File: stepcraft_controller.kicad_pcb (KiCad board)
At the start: 2 copper layers, 68 x 55 mm, 67 parts, among them J1 USB, J2 Probe, J3 Spindle, J4 CONN_01X03, J5 CONN_01X03, J6 Relay select, J7 Serial, J8 ISP, J9 X1, SW1 RST, U1 CP2102, U2 ADuM1201BR, U3 ADuM1201BR, U4 ATMEGA328P-AU, Y1 Crystal

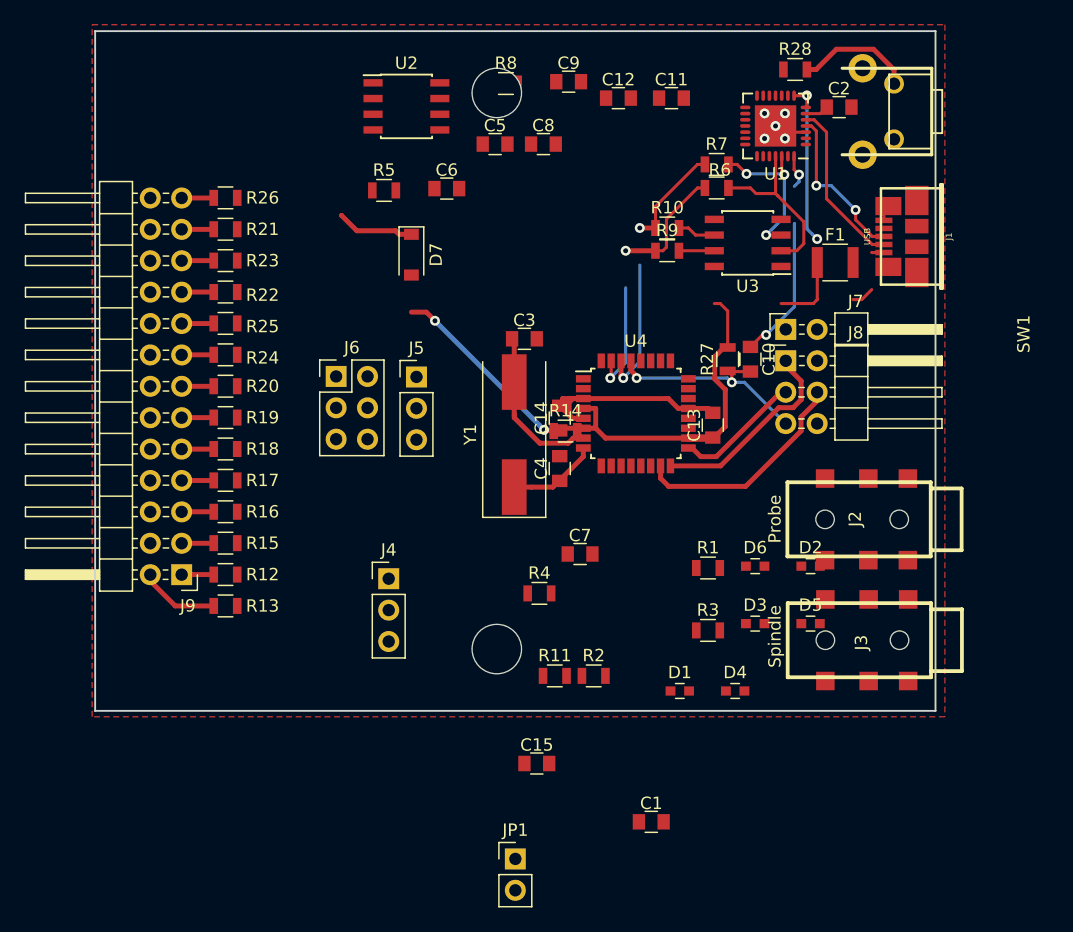
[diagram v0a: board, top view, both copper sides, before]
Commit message: Update schematics and board, fully routed board
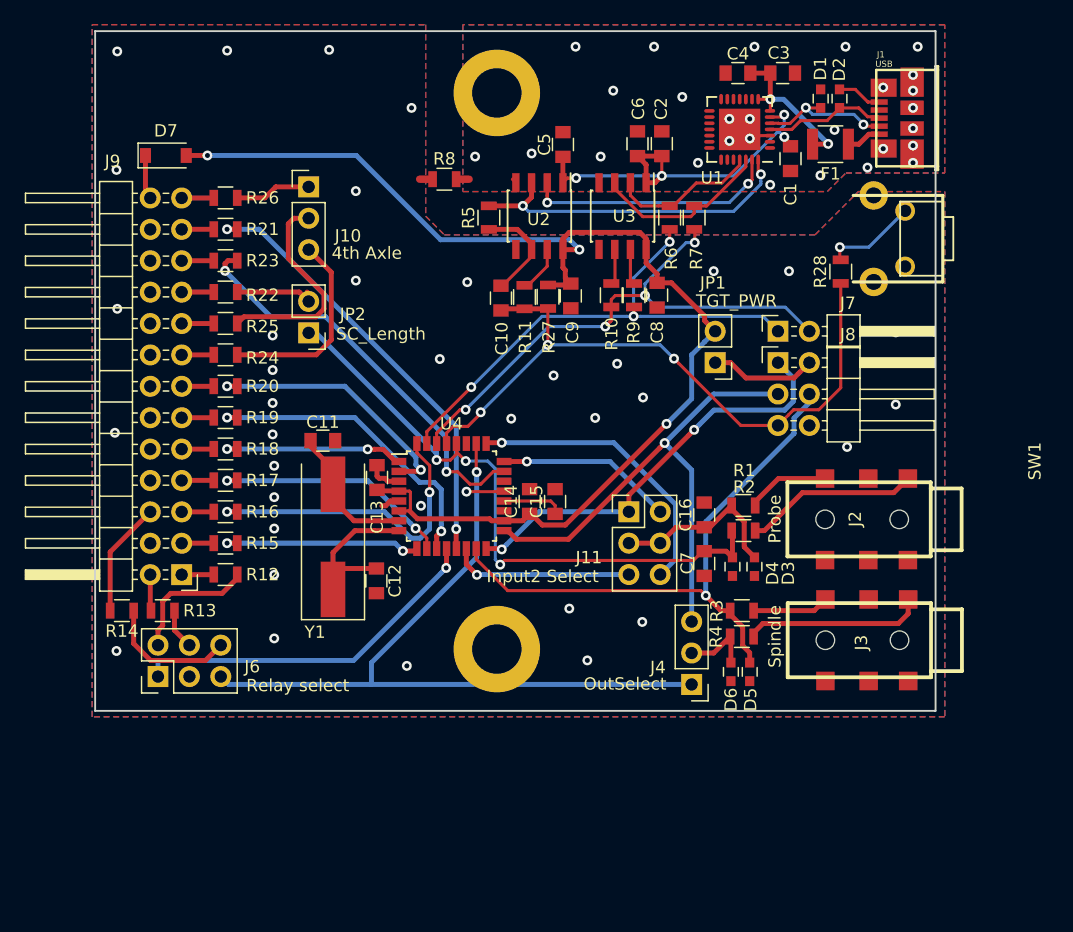
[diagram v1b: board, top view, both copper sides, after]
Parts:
- removed J5: CONN_01X03, Pin_Headers:Pin_Header_Straight_1x03_Pitch2.54mm
- added C16: 100n, Capacitors_SMD:C_0805, F.Cu at (189.3, 124.2)
- added J10: 4th Axle, Pin_Headers:Pin_Header_Straight_1x03_Pitch2.54mm, F.Cu at (157.3, 97.6)
- added J11: Input2 Select, Pin_Headers:Pin_Header_Straight_2x03_Pitch2.54mm, F.Cu at (183.2, 123.9)
- added JP2: SC_Length, Pin_Headers:Pin_Header_Straight_1x02_Pitch2.54mm, F.Cu at (157.3, 109.4)
- J1: footprint w_conn_pc:conn_usb_B_micro_smd -> iotta_footprints:conn_usb_B_micro_smd
- J4: value CONN_01X03 -> OutSelect
- moved C1 54.8 mm to (196.3, 95.3), turned to 270 degrees
- moved D1 49.3 mm to (198.7, 90.5), turned to 270 degrees
- moved C12 43.7 mm to (162.8, 129.5), turned to 270 degrees
- moved JP1 43.3 mm to (190.2, 111.8), turned to 180 degrees
- moved C11 39.5 mm to (158.4, 118.2)
- moved R14 38.7 mm to (142.2, 131.9), turned to 180 degrees
- moved D2 37.9 mm to (200.2, 90.5), turned to 270 degrees
- moved C4 35.1 mm to (192.0, 88.4), turned to 180 degrees
- moved R11 30.8 mm to (174.7, 106.5), turned to 270 degrees
- moved C3 30.0 mm to (195.6, 88.4)
- moved J6 28.2 mm to (145.1, 137.2), turned to 90 degrees
- moved C13 27.5 mm to (162.8, 121.1)
- moved J4 26.0 mm to (188.3, 137.9), turned to 180 degrees
- moved D7 21.4 mm to (145.7, 95.1), turned to 0 degrees
- moved C15 21.2 mm to (177.2, 123.1), turned to 90 degrees
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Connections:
- net Net-(C1-Pad1) renamed +5VP
- D3 pad 1: Net-(D3-Pad1) -> /Input2
- D4 pad 1: /Probe -> /A5
- D5 pad 1: /SpinPWM -> /D11_MOSI
- J2 pad 1: /Probe -> Net-(J2-Pad1)
- J2 pad 2: Net-(D3-Pad1) -> Net-(J2-Pad2)
- J3 pad 1: /SpinDir/Cool -> Net-(J3-Pad1)
- J3 pad 2: /SpinPWM -> Net-(J3-Pad2)
- J4 pad 2: Net-(J4-Pad2) -> /SpinDir/Cool
- J4 pad 3: /D13 -> /D13_SCK
- R1 pad 1: Net-(D3-Pad1) -> Net-(J2-Pad2)
- R1 pad 2: Net-(J5-Pad2) -> /Input2
- R2 pad 1: /Probe -> Net-(J2-Pad1)
- R21 pad 1: /D5 -> /D9
- R23 pad 1: Net-(R23-Pad1) -> /A0
- R3 pad 1: /SpinPWM -> Net-(J3-Pad2)
- R3 pad 2: /D11 -> /D11_MOSI
- R4 pad 1: /SpinDir/Cool -> Net-(J3-Pad1)
- R4 pad 2: Net-(J4-Pad2) -> /SpinDir/Cool
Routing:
- net /A3: track 0.00 -> 61.4 mm, vias 0 -> 1
- net +5V: track 44.4 -> 99.2 mm, vias 2 -> 3
- net /A5: track 0.00 -> 51.6 mm, vias 0 -> 3
- net /D9: track 0.00 -> 35.9 mm, vias 0 -> 2
- net /A0: track 0.00 -> 33.4 mm, vias 0 -> 2
- net /D13_SCK: track 10.3 -> 42.7 mm, vias 0 -> 1
- net +5VP: track 1.91 -> 34.2 mm, vias 0 -> 4
- net /D11_MOSI: track 18.2 -> 47.8 mm, vias 0 -> 1
- net /D8: track 0.00 -> 29.3 mm, vias 0 -> 1
- net /AVR_RX: track 19.6 -> 45.6 mm, vias 2 -> 4
- net /D2: track 0.00 -> 25.7 mm, vias 0 -> 2
- net /D7: track 0.00 -> 25.5 mm, vias 0 -> 2
- net /AVR_RST: track 29.7 -> 55.1 mm
- net Net-(R5-Pad2): track 2.76 -> 27.3 mm, vias 1 -> 2
- net /AVR_TX: track 19.1 -> 42.8 mm, vias 2 -> 3
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- added copper zone on F.Cu, net +5VP
- added copper zone on B.Cu, net GND
- added copper zone on F.Cu, net GND
- added copper zone on B.Cu, net GNDD

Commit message: Update PCB routing.
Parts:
- added REF**: Symbol_CreativeCommons_CopperTop_Type2_Small, Symbols:Symbol_CreativeCommons_CopperTop_Type2_Small, B.Cu at (146.4, 90.5)
- added REF**: Symbol_CC-Attribution_CopperTop_Small, Symbols:Symbol_CC-Attribution_CopperTop_Small, B.Cu at (159.1, 90.5)
- added REF**: Symbol_CC-Noncommercial_CopperTop_Small, Symbols:Symbol_CC-Noncommercial_CopperTop_Small, B.Cu at (152.7, 90.5)
- added REF***: OSHW-Symbol_6.7x6mm_SilkScreen, Symbols:OSHW-Symbol_6.7x6mm_SilkScreen, F.Cu at (180.4, 115.9)
- JP1: value TGT_PWR -> ISP_PWR
- SW1: value RST -> Reset
- moved F1 5.17 mm to (199.9, 89.0)
- moved J4 2.54 mm to (185.7, 137.9)
- moved D1 2.09 mm to (198.8, 92.6)
- moved D2 2.08 mm to (200.3, 92.6)
- moved C1 0.54 mm to (196.2, 95.9)
- moved C13 0.13 mm to (162.8, 121.3)
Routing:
- net Net-(F1-Pad2): track 2.83 -> 10.5 mm, vias 0 -> 2
- net /A3: track 61.4 -> 54.2 mm
- net GNDD: track 8.80 -> 14.7 mm, vias 37 -> 41
- net /SpinDir/Cool: track 5.80 -> 8.64 mm
- net /D4: track 21.5 -> 23.8 mm
- net /A5: track 51.6 -> 53.3 mm
- net /D7: track 25.5 -> 27.2 mm
- net Net-(U1-Pad27): track 22.1 -> 20.8 mm
- net /D13_SCK: track 42.7 -> 43.7 mm
- net /D9: track 35.9 -> 36.7 mm
- net Net-(R5-Pad2): track 27.3 -> 26.5 mm
- net /AVR_TX: track 42.8 -> 43.4 mm
- net +5VP: track 34.2 -> 34.8 mm
- net /A0: track 33.4 -> 34.1 mm
- net /AVR_RX: track 45.6 -> 45.0 mm
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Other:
- net class Default: clearance 0 -> 0.19
- rule trace_clearance: 0 -> 0.19
- board text added: "Rev 1.0 2017"
- board text added: "SC100 Drop-in replacement"
- board text added: "Stepcraft GRBLizer"

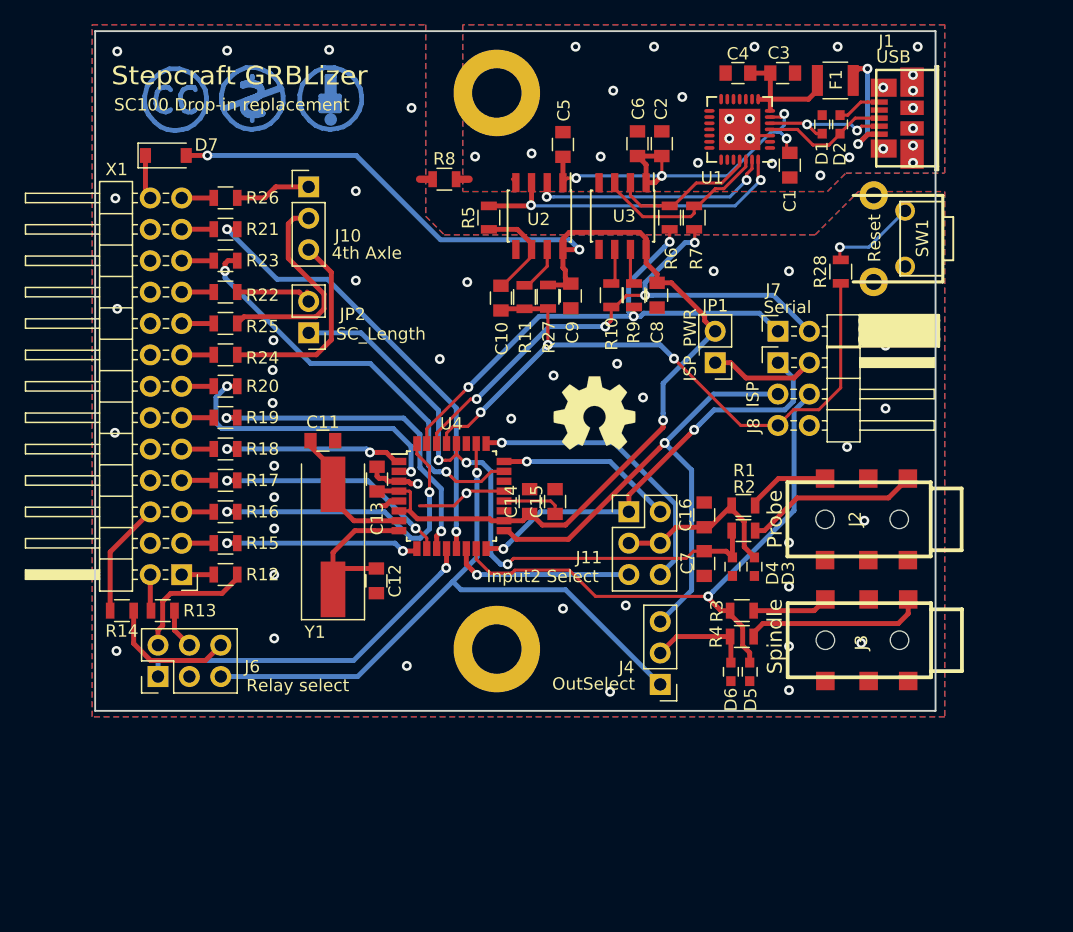
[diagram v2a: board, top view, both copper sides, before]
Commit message: Fix net name (D13), improved routing, ground plane continuity.
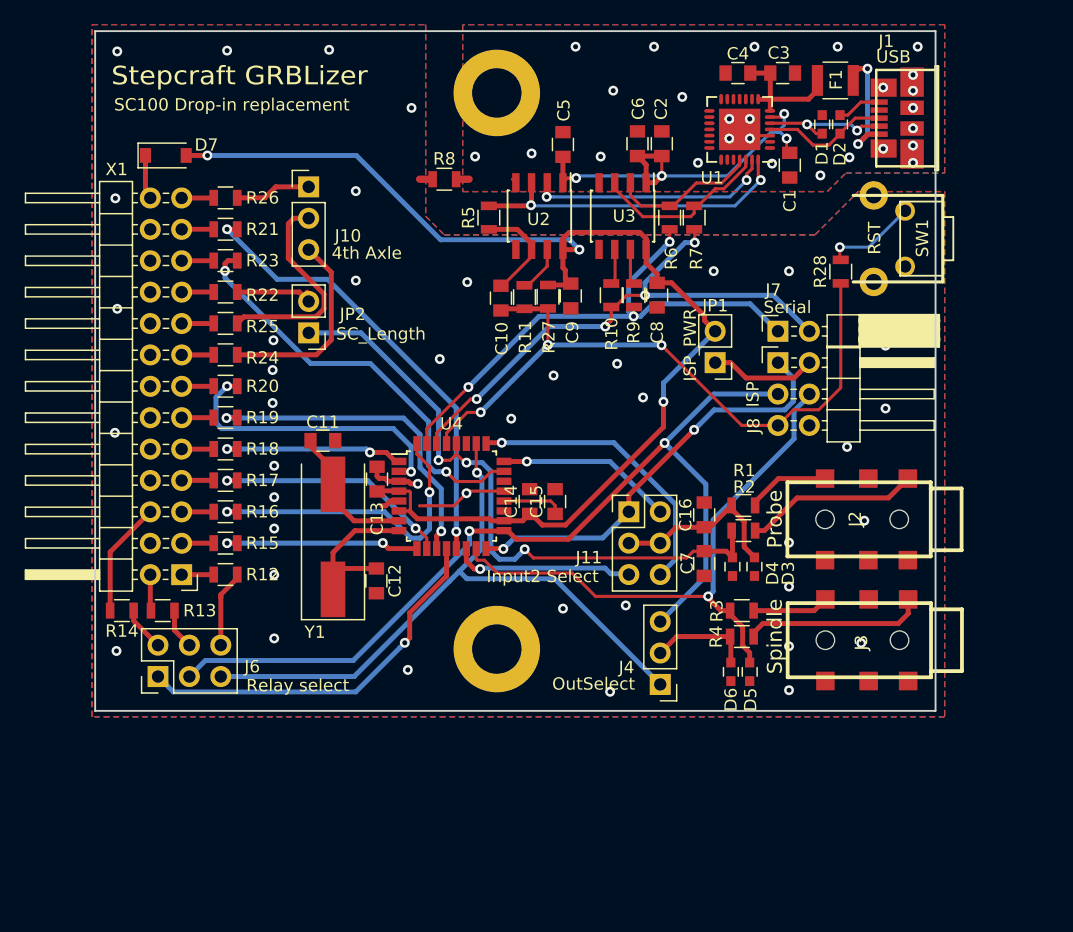
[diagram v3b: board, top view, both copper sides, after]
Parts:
- removed REF**: Symbol_CreativeCommons_CopperTop_Type2_Small, Symbols:Symbol_CreativeCommons_CopperTop_Type2_Small
- removed REF**: Symbol_CC-Attribution_CopperTop_Small, Symbols:Symbol_CC-Attribution_CopperTop_Small
- removed REF**: Symbol_CC-Noncommercial_CopperTop_Small, Symbols:Symbol_CC-Noncommercial_CopperTop_Small
- removed REF***: OSHW-Symbol_6.7x6mm_SilkScreen, Symbols:OSHW-Symbol_6.7x6mm_SilkScreen
- SW1: value Reset -> RST
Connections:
- J6 pad 3: /D13 -> /D13_SCK
- R12 pad 1: Net-(J6-Pad2) -> Net-(J6-Pad6)
- R14 pad 1: Net-(J6-Pad6) -> Net-(J6-Pad2)
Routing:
- net /D13_SCK: track 43.7 -> 75.7 mm, vias 1 -> 2
- net Net-(J6-Pad2): track 10.8 -> 3.61 mm
- net Net-(J6-Pad6): track 10.8 -> 6.27 mm
- net /D8: track 29.3 -> 31.2 mm
- net /AVR_TX: track 43.4 -> 44.1 mm

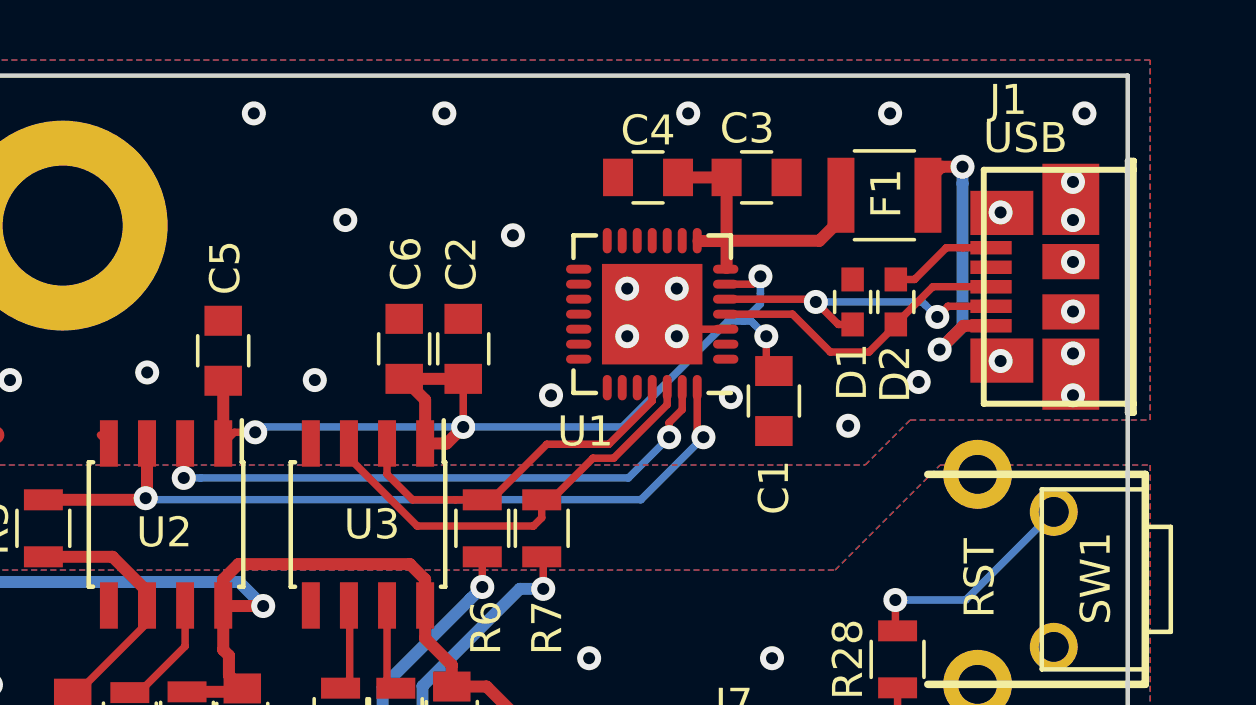
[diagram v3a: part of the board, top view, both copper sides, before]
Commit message: Change SiLabs CP2102 QFN-28 to (more common) CP2102N QFN-24
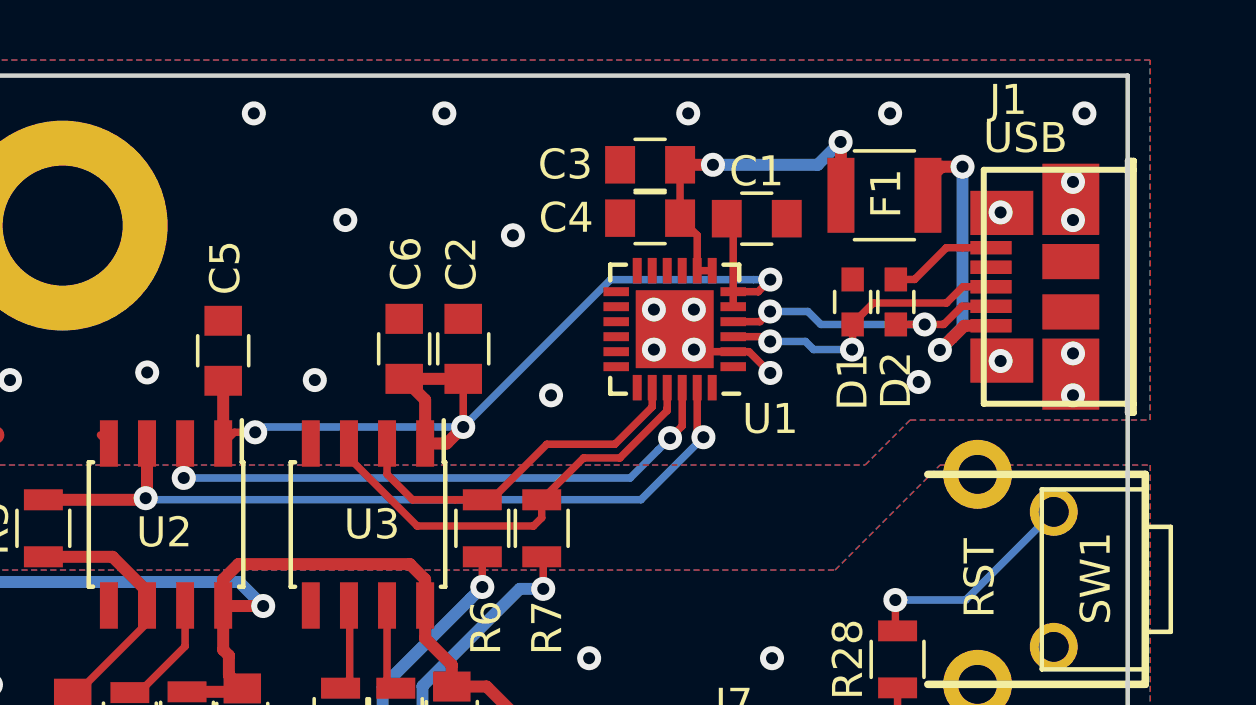
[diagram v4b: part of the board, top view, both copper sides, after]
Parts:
- U1: value CP2102 -> CP2102N-A01-GQFN24; footprint Housings_DFN_QFN:QFN-28-1EP_5x5mm_Pitch0.5mm -> Housings_DFN_QFN:QFN-24-1EP_4x4mm_Pitch0.5mm
- moved C1 6.11 mm to (195.6, 89.8), turned to 0 degrees
- moved C3 3.58 mm to (192.1, 88.0), turned to 180 degrees
- moved C4 1.36 mm to (192.1, 89.8)
- moved U1 0.90 mm to (192.9, 93.5)
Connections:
- J1 pad 2: Net-(D1-Pad2) -> Net-(D2-Pad2)
- J1 pad 3: Net-(D2-Pad2) -> Net-(D1-Pad2)
- U1 pad 2: Net-(U1-Pad2) -> GND
- U1 pad 20: Net-(U1-Pad20) -> Net-(R6-Pad2)
- U1 pad 21: Net-(U1-Pad21) -> Net-(R7-Pad2)
- U1 pad 23: Net-(U1-Pad23) -> Net-(R5-Pad2)
- U1 pad 25: Net-(R6-Pad2) -> GND
- U1 pad 3: GND -> Net-(D1-Pad2)
- U1 pad 5: Net-(D1-Pad2) -> +5VP
- U2 pad 2: Net-(U1-Pad27) -> Net-(U1-Pad22)
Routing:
- net Net-(U1-Pad22): track 0.00 -> 20.8 mm, vias 0 -> 2
- net Net-(U1-Pad27): track 20.8 -> 0.00 mm, vias 2 -> 0
- net GND: track 6.79 -> 7.93 mm, vias 24 -> 23
- net Net-(C3-Pad1): track 12.6 -> 11.7 mm, vias 0 -> 2
- net +5VP: track 34.8 -> 35.5 mm, vias 4 -> 3
- net Net-(D1-Pad2): track 10.8 -> 10.2 mm
- net Net-(D2-Pad2): track 10.3 -> 10.2 mm, vias 0 -> 2
- net (no net): vias 2 -> 0
